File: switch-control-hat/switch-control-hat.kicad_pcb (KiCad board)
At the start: 2 copper layers, 85 x 56 mm, 40 parts, among them J1 Frontend Connector, J2 Power Connector, J3 Conn_01x02, P1 RPi-Header, U1 TLP3543, U2 TLP3543, U3 TLP3543, U4 TLP3543, U5 TLP3543, U6 TLP3543, U7 TLP3543, U8 TLP3543, U9 DS3231M

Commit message: final version
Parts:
- added J4: Power Connector, Connector_Phoenix_MC:PhoenixContact_MC_1,5_3-G-3.81_1x03_P3.81mm_Horizontal, F.Cu at (270.7, 145.7)
- added SW1: SW_Push, Button_Switch_SMD:SW_Push_SPST_NO_Alps_SKRK, F.Cu at (281.7, 134.3)
- D1, D2, D3, D4, D5, D6, D7, D8: footprint Diode_THT:D_DO-41_SOD81_P3.81mm_Vertical_KathodeUp -> Diode_THT:D_DO-41_SOD81_P3.81mm_Vertical_AnodeUp
- J1: value Frontend Connector -> Conn_01x09; footprint Connector_Phoenix_MC:PhoenixContact_MC_1,5_12-G-3.81_1x12_P3.81mm_Horizontal -> Connector_PinSocket_2.54mm:PinSocket_1x09_P2.54mm_Vertical
- J2: value Power Connector -> Frontend Connector; footprint Connector_Phoenix_MC:PhoenixContact_MC_1,5_3-G-3.81_1x03_P3.81mm_Horizontal -> Connector_Phoenix_MC:PhoenixContact_MC_1,5_12-G-3.81_1x12_P3.81mm_Horizontal
- R3: value 200 -> 4K7
- R9: value 4K7 -> 200
- moved J2 59.7 mm to (211.4, 145.7)
- moved R13 59.6 mm to (269.1, 128.0), turned to 180 degrees
- moved J1 39.0 mm to (203.9, 106.8)
- moved R7 22.5 mm to (236.4, 122.1)
- moved R5 21.7 mm to (222.5, 122.1)
- moved R9 17.9 mm to (250.4, 122.1), turned to 0 degrees
- moved R8 13.5 mm to (250.4, 106.8)
- moved R6 13.4 mm to (236.4, 106.8)
- moved R4 13.3 mm to (222.5, 106.8)
- moved D8 5.47 mm to (257.1, 139.8), turned to 90 degrees
- moved D7 5.47 mm to (249.5, 139.8), turned to 90 degrees
- moved D2 5.38 mm to (215.2, 139.8), turned to 90 degrees
- moved D1 5.38 mm to (207.6, 139.8), turned to 90 degrees
- moved D5 5.14 mm to (235.6, 139.8), turned to 90 degrees
- moved D6 5.14 mm to (243.2, 139.8), turned to 90 degrees
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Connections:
- D1 pad 1: GND -> /POS1
- D1 pad 2: /POS1 -> GND
- D2 pad 1: GND -> /POS2
- D2 pad 2: /POS2 -> GND
- D3 pad 1: GND -> /POS3
- D3 pad 2: /POS3 -> GND
- D4 pad 1: GND -> /POS4
- D4 pad 2: /POS4 -> GND
- D5 pad 1: GND -> /POS5
- D5 pad 2: /POS5 -> GND
- D6 pad 1: GND -> /POS6
- D6 pad 2: /POS6 -> GND
- D7 pad 1: GND -> /RESET
- D7 pad 2: /RESET -> GND
- D8 pad 1: GND -> /NOISE-DIODE
- D8 pad 2: /NOISE-DIODE -> GND
- J1 pad 1: /POS1 -> (no net)
- J1 pad 2: /POS2 -> (no net)
- J1 pad 3: /ONE-WIRE -> (no net)
- J1 pad 4: /POS3 -> (no net)
- J1 pad 5: /POS4 -> /GPIO15(RXD0)
- J1 pad 6: GND -> /GPIO14(TXD0)
- J1 pad 7: +12V -> GND
- J1 pad 8: /POS5 -> +3V3
- J1 pad 9: /POS6 -> (no net)
- J2 pad 1: +15V -> /POS1
- J2 pad 2: +12V -> /POS2
- J2 pad 3: (no net) -> /ONE-WIRE
- P1 pad 10: (no net) -> /GPIO15(RXD0)
- P1 pad 17: +3V3 -> (no net)
- P1 pad 2: +5V -> (no net)
- P1 pad 4: +5V -> (no net)
- P1 pad 8: (no net) -> /GPIO14(TXD0)
- R10 pad 1: Net-(J3-Pad2) -> +3V3
- R10 pad 2: +3V3 -> /GPIO3(SCL1)
- R11 pad 2: /GPIO3(SCL1) -> /GPIO2(SDA1)
- R12 pad 1: +3V3 -> Net-(J3-Pad2)
- R12 pad 2: /GPIO2(SDA1) -> +3V3
- R13 pad 1: +3V3 -> Net-(J3-Pad1)
- R13 pad 2: /ONE-WIRE -> +3V3
- R3 pad 1: Net-(R3-Pad1) -> +3V3
- R3 pad 2: /GPIO13(PWM1) -> /ONE-WIRE
- R4 pad 2: /GPIO16 -> /GPIO13(PWM1)
- R5 pad 2: /GPIO19(SPI1_MISO) -> /GPIO16
- R6 pad 2: /GPIO20(SPI1_MOSI) -> /GPIO19(SPI1_MISO)
- R7 pad 2: /GPIO26 -> /GPIO20(SPI1_MOSI)
- R8 pad 2: /GPIO21(SPI1_SCK) -> /GPIO26
- R9 pad 1: Net-(J3-Pad1) -> Net-(R9-Pad1)
- R9 pad 2: +3V3 -> /GPIO21(SPI1_SCK)
- U3 pad 1: Net-(R3-Pad1) -> Net-(R4-Pad1)
- U4 pad 1: Net-(R4-Pad1) -> Net-(R5-Pad1)
- U5 pad 1: Net-(R5-Pad1) -> Net-(R6-Pad1)
- U6 pad 1: Net-(R6-Pad1) -> Net-(R7-Pad1)
- U7 pad 1: Net-(R7-Pad1) -> Net-(R8-Pad1)
- U8 pad 1: Net-(R8-Pad1) -> Net-(R9-Pad1)
- U9 pad 4: (no net) -> Net-(SW1-Pad1)
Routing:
- net /GPIO14(TXD0): track 0.00 -> 35.1 mm
- net /GPIO15(RXD0): track 0.00 -> 34.1 mm
- net Net-(BT1-Pad1): track 33.6 -> 6.81 mm
- net +12V: track 234.7 -> 218.0 mm
- net Net-(SW1-Pad1): track 0.00 -> 7.05 mm
- net Net-(R9-Pad1): track 0.00 -> 5.08 mm
- net Net-(R3-Pad1): track 4.44 -> 0.00 mm
- net /GPIO6: track 45.3 -> 41.3 mm
- net /GPIO12(PWM0): track 63.4 -> 60.1 mm
- net /GPIO2(SDA1): track 84.6 -> 81.5 mm
- net /POS2: track 24.0 -> 21.1 mm
- net /NOISE-DIODE: track 24.5 -> 21.6 mm
- net +5V: track 2.54 -> 0.00 mm
- net +15V: track 36.2 -> 33.6 mm
- net /POS4: track 23.3 -> 21.1 mm
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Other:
- outline, holes or cut-outs redrawn
- board text added: "NIvek Ghazi Tankiso Moso Cynthia Chiang Jonathan Sievers Liju Phillip Veruschka Simes Scott Eyono"
- board text added: "PRIZM Control Circuit V1.1"
- board text removed: "12V"
- board text removed: "GND"
- board text removed: "NS"
- board text removed: "P1"
- board text removed: "P2"
- board text removed: "P3"
- board text removed: "P4"
- board text removed: "P5"
- board text removed: "P6"
- board text removed: "PRIZM switch control v1.1"
- board text removed: "RST"
- board text removed: "TEMP"
- board text removed: "Tankiso H. Moso Liju Phillip Cynthia Chiang Jonathan Sievers Nivek Ghazi Scott Eyono"

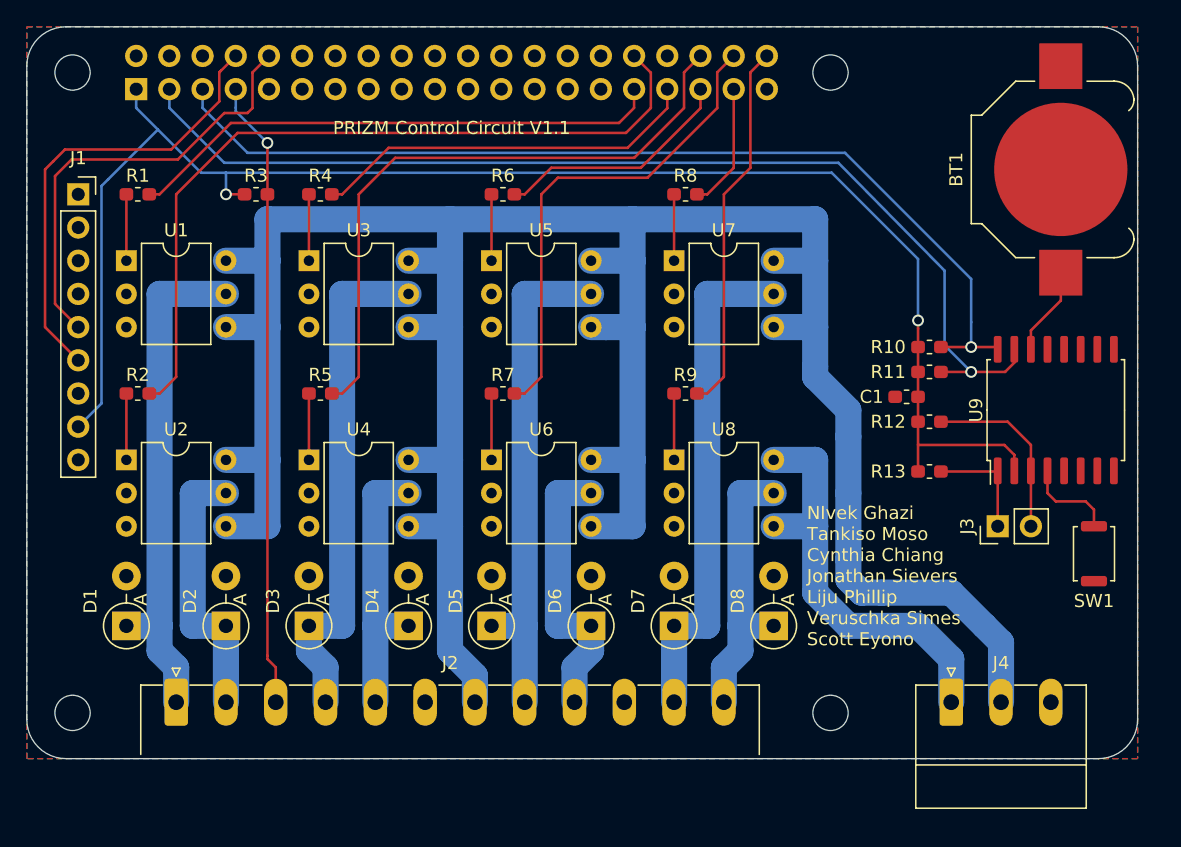
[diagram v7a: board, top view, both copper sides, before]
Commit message: Updated to control second frontend switch
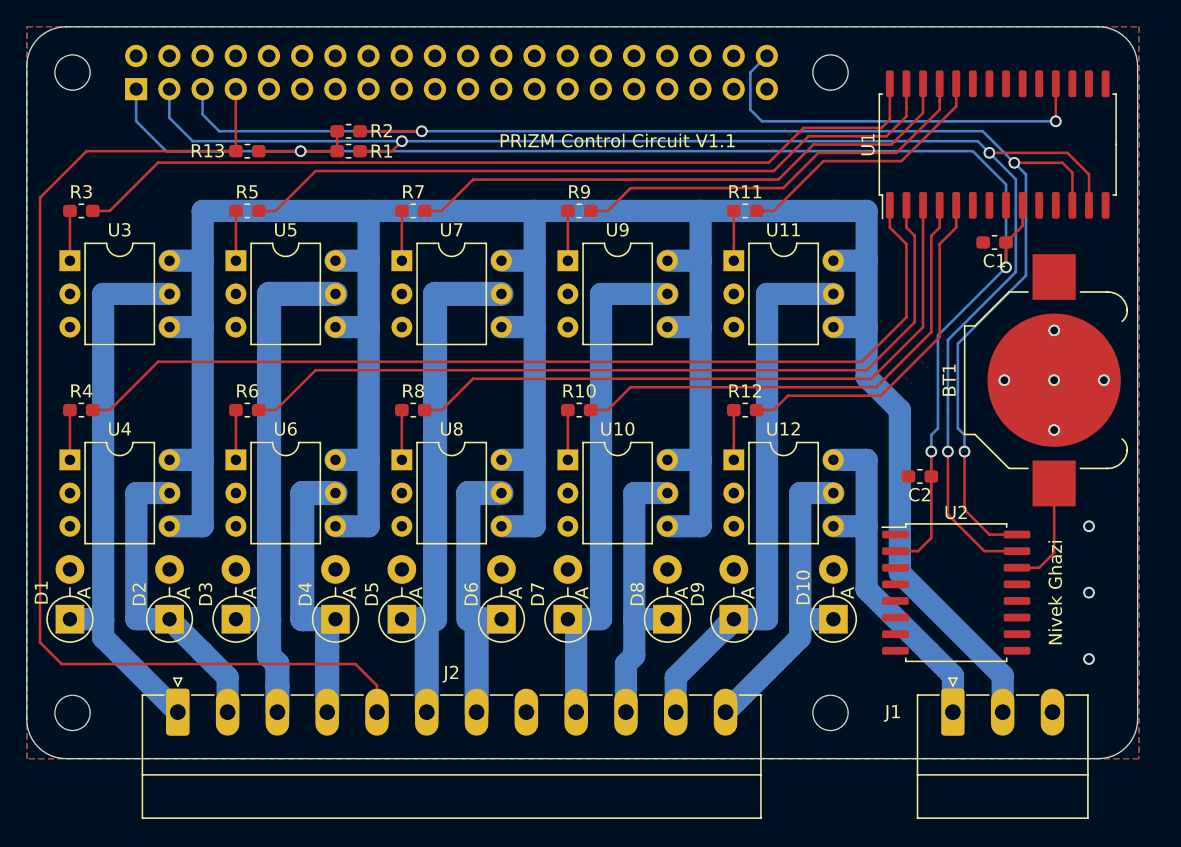
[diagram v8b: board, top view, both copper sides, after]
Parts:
- removed J3: Conn_01x02, Connector_PinHeader_2.54mm:PinHeader_1x02_P2.54mm_Vertical
- removed J4: Power Connector, Connector_Phoenix_MC:PhoenixContact_MC_1,5_3-G-3.81_1x03_P3.81mm_Horizontal
- removed SW1: SW_Push, Button_Switch_SMD:SW_Push_SPST_NO_Alps_SKRK
- added C2: 1uF, Capacitor_SMD:C_0603_1608Metric_Pad1.05x0.95mm_HandSolder, F.Cu at (268.3, 128.4)
- added D10: 1N4001, Diode_THT:D_DO-41_SOD81_P3.81mm_Vertical_AnodeUp, F.Cu at (261.7, 139.3)
- added D9: 1N4001, Diode_THT:D_DO-41_SOD81_P3.81mm_Vertical_AnodeUp, F.Cu at (254.1, 139.3)
- added U10: TLP3543, Package_DIP:DIP-6_W7.62mm, F.Cu at (241.4, 127.1)
- added U11: TLP3543, Package_DIP:DIP-6_W7.62mm, F.Cu at (254.1, 111.9)
- added U12: TLP3543, Package_DIP:DIP-6_W7.62mm, F.Cu at (254.1, 127.1)
- C1: value 1uF -> C
- J1: value Conn_01x09 -> Power Connector; footprint Connector_PinSocket_2.54mm:PinSocket_1x09_P2.54mm_Vertical -> Connector_Phoenix_MC:PhoenixContact_MC_1,5_3-G-3.81_1x03_P3.81mm_Horizontal
- R1, R2: value 200 -> 4K7
- R10, R11, R12, R3: value 4K7 -> 200
- U1: value TLP3543 -> MCP23017_SO; footprint Package_DIP:DIP-6_W7.62mm -> Package_SO:SOIC-28W_7.5x17.9mm_P1.27mm
- U2: value TLP3543 -> DS3231M; footprint Package_DIP:DIP-6_W7.62mm -> Package_SO:SOIC-16W_7.5x10.3mm_P1.27mm
- U9: value DS3231M -> TLP3543; footprint Package_SO:SOIC-16W_7.5x10.3mm_P1.27mm -> Package_DIP:DIP-6_W7.62mm
- moved J1 77.8 mm to (270.9, 146.4)
- moved U1 67.3 mm to (274.3, 103.0), turned to 90 degrees
- moved U2 64.3 mm to (271.1, 137.3)
- moved R13 57.7 mm to (216.9, 103.5)
- moved U9 39.0 mm to (241.4, 111.9), turned to 0 degrees
- moved R10 27.2 mm to (242.3, 123.3)
- moved R8 26.6 mm to (229.6, 123.3)
- moved R2 25.7 mm to (224.6, 102.0)
- moved R6 25.6 mm to (216.9, 123.3)
- moved R4 24.6 mm to (204.2, 123.3)
- moved U7 20.8 mm to (228.7, 111.9)
- moved U8 20.8 mm to (228.7, 127.1)
- moved U5 19.6 mm to (216.0, 111.9)
- moved U6 19.6 mm to (216.0, 127.1)
- moved R11 18.7 mm to (255.0, 108.1)
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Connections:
- D1 pad 1: /POS1 -> /output_connectors/POS_1
- D2 pad 1: /POS2 -> /output_connectors/POS_2
- D3 pad 1: /POS3 -> /output_connectors/POS_3
- D4 pad 1: /POS4 -> /output_connectors/POS_4
- D5 pad 1: /POS5 -> /output_connectors/POS_5
- D6 pad 1: /POS6 -> /output_connectors/POS_6
- D7 pad 1: /RESET -> /output_connectors/RESET
- D8 pad 1: /NOISE-DIODE -> /output_connectors/ANTENNA
- J1 pad 1: (no net) -> +15V
- J1 pad 2: (no net) -> +12V
- J1 pad 3: (no net) -> GND
- J2 pad 1: /POS1 -> /output_connectors/POS_1
- J2 pad 10: GND -> /output_connectors/ANTENNA
- J2 pad 11: /RESET -> /output_connectors/VNA
- J2 pad 12: /NOISE-DIODE -> /output_connectors/NOISE-SOURCE
- J2 pad 2: /POS2 -> /output_connectors/POS_2
- J2 pad 3: /ONE-WIRE -> /output_connectors/POS_3
- J2 pad 4: /POS3 -> /output_connectors/POS_4
- J2 pad 5: /POS4 -> /output_connectors/ONE-WIRE
- J2 pad 6: GND -> /output_connectors/POS_5
- J2 pad 7: +12V -> /output_connectors/POS_6
- J2 pad 8: /POS5 -> GND
- J2 pad 9: /POS6 -> /output_connectors/RESET
- P1 pad 10: /GPIO15(RXD0) -> Net-(P1-Pad10)
- P1 pad 11: (no net) -> Net-(P1-Pad11)
- P1 pad 12: (no net) -> Net-(P1-Pad12)
- P1 pad 13: (no net) -> Net-(P1-Pad13)
- P1 pad 15: (no net) -> Net-(P1-Pad15)
- P1 pad 16: (no net) -> Net-(P1-Pad16)
- P1 pad 17: (no net) -> Net-(P1-Pad17)
- P1 pad 18: (no net) -> Net-(P1-Pad18)
- P1 pad 19: (no net) -> Net-(P1-Pad19)
- P1 pad 2: (no net) -> Net-(P1-Pad2)
- P1 pad 21: (no net) -> Net-(P1-Pad21)
- P1 pad 22: (no net) -> Net-(P1-Pad22)
- P1 pad 23: (no net) -> Net-(P1-Pad23)
- P1 pad 24: (no net) -> Net-(P1-Pad24)
- P1 pad 26: (no net) -> Net-(P1-Pad26)
- P1 pad 27: (no net) -> Net-(P1-Pad27)
- P1 pad 28: (no net) -> Net-(P1-Pad28)
- P1 pad 29: (no net) -> Net-(P1-Pad29)
- P1 pad 3: /GPIO2(SDA1) -> /i2c_expander/I2C_SDA
- P1 pad 31: /GPIO6 -> Net-(P1-Pad31)
- P1 pad 32: /GPIO12(PWM0) -> Net-(P1-Pad32)
- P1 pad 33: /GPIO13(PWM1) -> Net-(P1-Pad33)
- P1 pad 35: /GPIO19(SPI1_MISO) -> Net-(P1-Pad35)
- P1 pad 36: /GPIO16 -> Net-(P1-Pad36)
- P1 pad 37: /GPIO26 -> Net-(P1-Pad37)
- P1 pad 38: /GPIO20(SPI1_MOSI) -> Net-(P1-Pad38)
- P1 pad 4: (no net) -> Net-(P1-Pad4)
- P1 pad 40: /GPIO21(SPI1_SCK) -> /i2c_expander/~RESET
- P1 pad 5: /GPIO3(SCL1) -> /i2c_expander/I2C_SCL
- P1 pad 7: /ONE-WIRE -> /output_connectors/ONE-WIRE
- P1 pad 8: /GPIO14(TXD0) -> Net-(P1-Pad8)
- R1 pad 1: Net-(R1-Pad1) -> +3V3
- R1 pad 2: /GPIO6 -> /i2c_expander/I2C_SDA
- R10 pad 1: +3V3 -> Net-(R10-Pad1)
- R10 pad 2: /GPIO3(SCL1) -> /i2c_expander/S2_POS_1
- R11 pad 1: +3V3 -> Net-(R11-Pad1)
- R11 pad 2: /GPIO2(SDA1) -> /i2c_expander/S2_POS_2
- R12 pad 1: Net-(J3-Pad2) -> Net-(R12-Pad1)
- R12 pad 2: +3V3 -> /i2c_expander/NOISE_ON
- R13 pad 1: Net-(J3-Pad1) -> +3V3
- R13 pad 2: +3V3 -> /output_connectors/ONE-WIRE
- R2 pad 1: Net-(R2-Pad1) -> +3V3
- R2 pad 2: /GPIO12(PWM0) -> /i2c_expander/I2C_SCL
- R3 pad 1: +3V3 -> Net-(R3-Pad1)
- R3 pad 2: /ONE-WIRE -> /i2c_expander/S1_POS_1
- R4 pad 2: /GPIO13(PWM1) -> /i2c_expander/S1_POS_2
- R5 pad 2: /GPIO16 -> /i2c_expander/S1_POS_3
- R6 pad 2: /GPIO19(SPI1_MISO) -> /i2c_expander/S1_POS_4
- R7 pad 2: /GPIO20(SPI1_MOSI) -> /i2c_expander/S1_POS_5
- R8 pad 2: /GPIO26 -> /i2c_expander/S1_POS_6
- R9 pad 2: /GPIO21(SPI1_SCK) -> /i2c_expander/S1_RESET
- U1 pad 1: Net-(R1-Pad1) -> /i2c_expander/S1_POS_2
- U1 pad 2: GND -> /i2c_expander/S1_POS_4
- U1 pad 3: (no net) -> /i2c_expander/S1_POS_6
- U1 pad 4: +12V -> /i2c_expander/S2_POS_1
- U1 pad 5: /POS1 -> /i2c_expander/NOISE_ON
- U1 pad 6: +12V -> Net-(U1-Pad6)
- U2 pad 1: Net-(R2-Pad1) -> Net-(U2-Pad1)
- U2 pad 2: GND -> +3V3
- U2 pad 3: (no net) -> Net-(U2-Pad3)
- U2 pad 4: +12V -> Net-(U2-Pad4)
- U2 pad 5: /POS2 -> GND
- U2 pad 6: +12V -> GND
- U3 pad 1: Net-(R4-Pad1) -> Net-(R3-Pad1)
- U3 pad 3: (no net) -> Net-(U3-Pad3)
- U3 pad 5: /POS3 -> /output_connectors/POS_1
- U4 pad 1: Net-(R5-Pad1) -> Net-(R4-Pad1)
- U4 pad 3: (no net) -> Net-(U4-Pad3)
- U4 pad 5: /POS4 -> /output_connectors/POS_2
- U5 pad 1: Net-(R6-Pad1) -> Net-(R5-Pad1)
- U5 pad 3: (no net) -> Net-(U5-Pad3)
- U5 pad 5: /POS5 -> /output_connectors/POS_3
- U6 pad 1: Net-(R7-Pad1) -> Net-(R6-Pad1)
- U6 pad 3: (no net) -> Net-(U6-Pad3)
- U6 pad 5: /POS6 -> /output_connectors/POS_4
- U7 pad 1: Net-(R8-Pad1) -> Net-(R7-Pad1)
- U7 pad 3: (no net) -> Net-(U7-Pad3)
- U7 pad 5: /RESET -> /output_connectors/POS_5
- U8 pad 1: Net-(R9-Pad1) -> Net-(R8-Pad1)
- U8 pad 3: (no net) -> Net-(U8-Pad3)
- U8 pad 4: +15V -> +12V
- U8 pad 5: /NOISE-DIODE -> /output_connectors/POS_6
- U8 pad 6: +15V -> +12V
- U9 pad 1: Net-(J3-Pad1) -> Net-(R9-Pad1)
- U9 pad 2: +3V3 -> GND
- U9 pad 3: Net-(J3-Pad2) -> Net-(U9-Pad3)
- U9 pad 4: Net-(SW1-Pad1) -> +12V
- U9 pad 5: GND -> /output_connectors/RESET
- U9 pad 6: GND -> +12V
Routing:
- net /i2c_expander/I2C_SDA: track 0.00 -> 117.4 mm, vias 0 -> 3
- net /i2c_expander/I2C_SCL: track 0.00 -> 111.6 mm, vias 0 -> 3
- net /output_connectors/ONE-WIRE: track 0.00 -> 84.4 mm
- net /GPIO2(SDA1): track 81.5 -> 0.00 mm, vias 1 -> 0
- net /GPIO3(SCL1): track 75.3 -> 0.00 mm, vias 1 -> 0
- net /i2c_expander/S1_POS_2: track 0.00 -> 74.8 mm
- net /i2c_expander/S1_POS_1: track 0.00 -> 66.7 mm
- net /i2c_expander/S1_POS_4: track 0.00 -> 62.2 mm
- net /GPIO12(PWM0): track 60.1 -> 0.00 mm
- net /i2c_expander/S1_POS_3: track 0.00 -> 55.0 mm
- net /i2c_expander/S1_POS_6: track 0.00 -> 50.1 mm
- net /GPIO16: track 48.7 -> 0.00 mm
- net /ONE-WIRE: track 48.2 -> 0.00 mm, vias 1 -> 0
- net /i2c_expander/S1_POS_5: track 0.00 -> 43.5 mm
- net /output_connectors/POS_1: track 0.00 -> 42.0 mm
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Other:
- board text added: "Nivek Ghazi"
- board text removed: "NIvek Ghazi Tankiso Moso Cynthia Chiang Jonathan Sievers Liju Phillip Veruschka Simes Scott Eyono"
